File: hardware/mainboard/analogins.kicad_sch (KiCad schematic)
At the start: 27 parts, among them J102 CASTOR PITCH, J103 CASTOR DUTY, J111 POLLUX PITCH, J112 POLLUX DUTY, U13 MCP6004

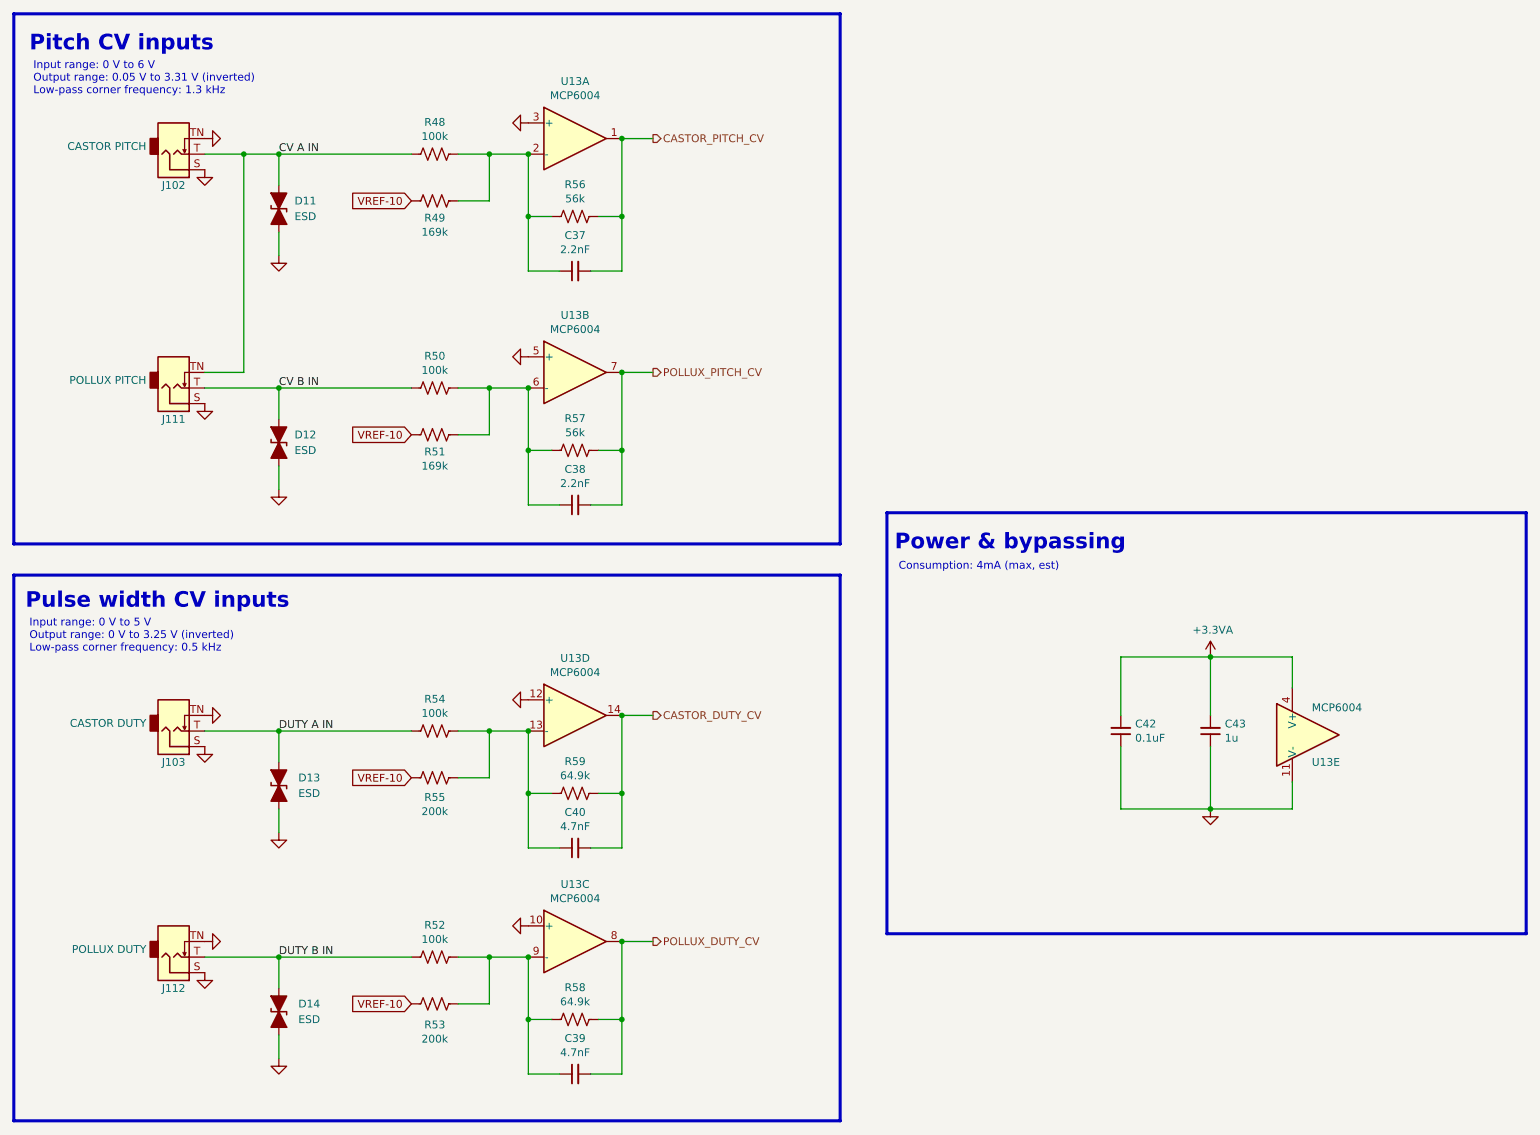
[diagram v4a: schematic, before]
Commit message: Reannotate schematic
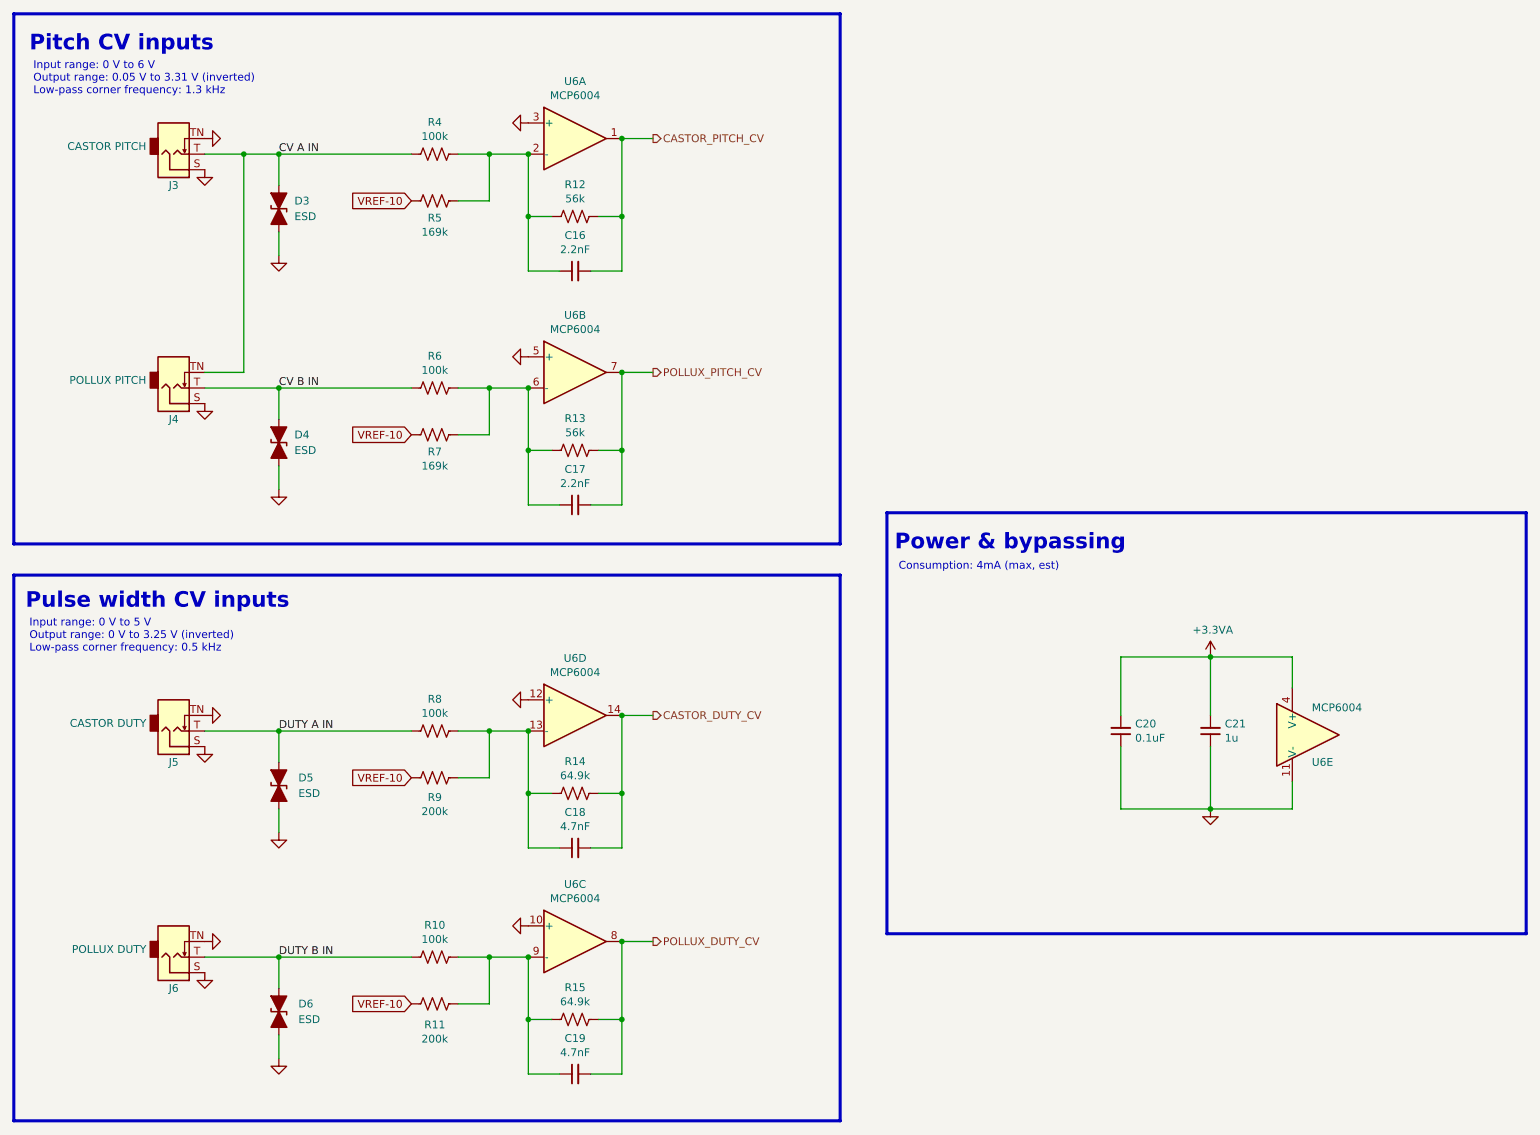
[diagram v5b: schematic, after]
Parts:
- renumbered C37 to C16, C38 to C17, C40 to C18, C39 to C19, C42 to C20, C43 to C21, D11 to D3, D12 to D4, D13 to D5, D14 to D6, J102 to J3, J111 to J4, J103 to J5, J112 to J6, R52 to R10, R53 to R11, R56 to R12, R57 to R13, R59 to R14, R58 to R15, R48 to R4, R49 to R5, R50 to R6, R51 to R7, R54 to R8, R55 to R9, U13 to U6

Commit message: Normalize component values
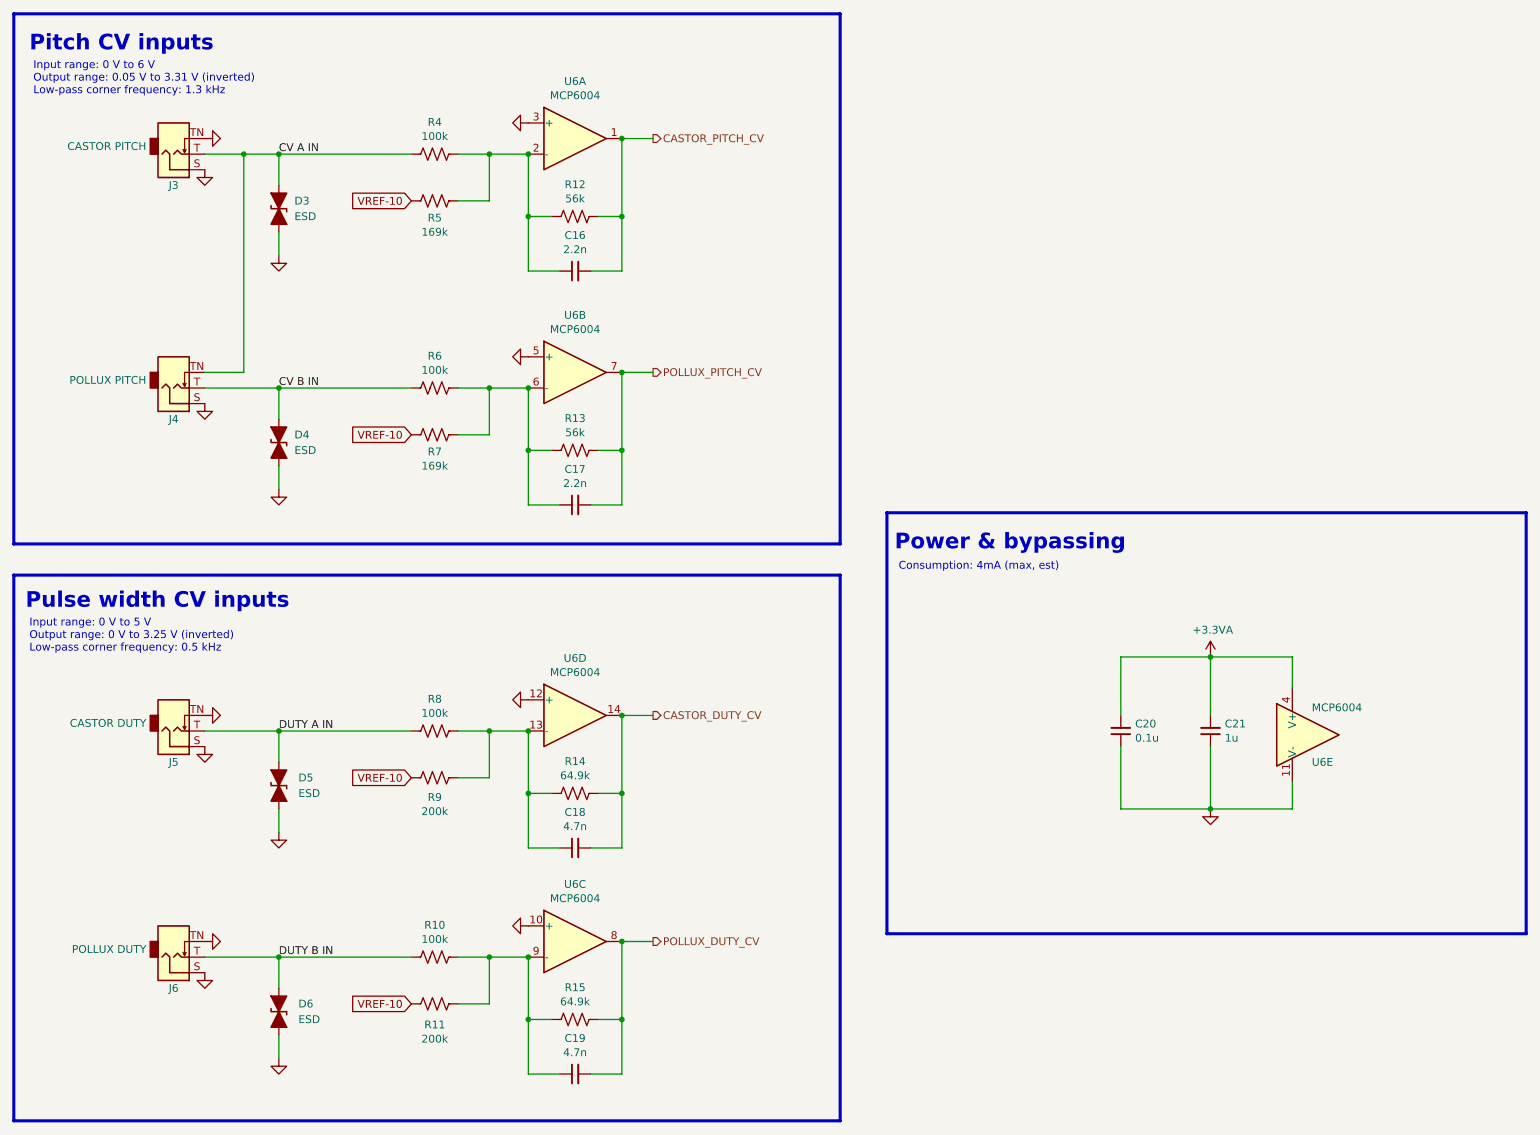
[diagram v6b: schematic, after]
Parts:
- C16, C17: value 2.2nF -> 2.2n
- C18, C19: value 4.7nF -> 4.7n
- C20: value 0.1uF -> 0.1u
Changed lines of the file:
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@@
     (in_bom yes) (on_board yes)
     (property "Reference" "C16" (id 0) (at 109.22 53.8734 90))
-    (property "Value" "2.2nF" (id 1) (at 109.22 56.1848 90))
+    (property "Value" "2.2n" (id 1) (at 109.22 56.1848 90))
     (property "Footprint" "Capacitor_SMD:C_0402_1005Metric_Pad0.74x0.62mm_HandSolder" (id 2) (at 109.22 59.69 0)
       (effects (font (size 1.27 1.27)) hide)
@@
     (in_bom yes) (on_board yes)
     (property "Reference" "C17" (id 0) (at 109.22 91.9734 90))
-    (property "Value" "2.2nF" (id 1) (at 109.22 94.2848 90))
+    (property "Value" "2.2n" (id 1) (at 109.22 94.2848 90))
     (property "Footprint" "Capacitor_SMD:C_0402_1005Metric_Pad0.74x0.62mm_HandSolder" (id 2) (at 109.22 97.79 0)
       (effects (font (size 1.27 1.27)) hide)
@@
     (in_bom yes) (on_board yes)
     (property "Reference" "C18" (id 0) (at 109.22 147.8534 90))
-    (property "Value" "4.7nF" (id 1) (at 109.22 150.1648 90))
+    (property "Value" "4.7n" (id 1) (at 109.22 150.1648 90))
     (property "Footprint" "Capacitor_SMD:C_0402_1005Metric_Pad0.74x0.62mm_HandSolder" (id 2) (at 109.22 153.67 0)
       (effects (font (size 1.27 1.27)) hide)
@@
     (in_bom yes) (on_board yes)
     (property "Reference" "C19" (id 0) (at 109.22 184.6834 90))
-    (property "Value" "4.7nF" (id 1) (at 109.22 186.9948 90))
+    (property "Value" "4.7n" (id 1) (at 109.22 186.9948 90))
     (property "Footprint" "Capacitor_SMD:C_0402_1005Metric_Pad0.74x0.62mm_HandSolder" (id 2) (at 109.22 190.5 0)
       (effects (font (size 1.27 1.27)) hide)
@@
       (effects (font (size 1.27 1.27)) (justify right))
     )
-    (property "Value" "0.1uF" (id 1) (at 200.4568 135.763 0)
+    (property "Value" "0.1u" (id 1) (at 200.4568 135.763 0)
       (effects (font (size 1.27 1.27)) (justify right))
     )

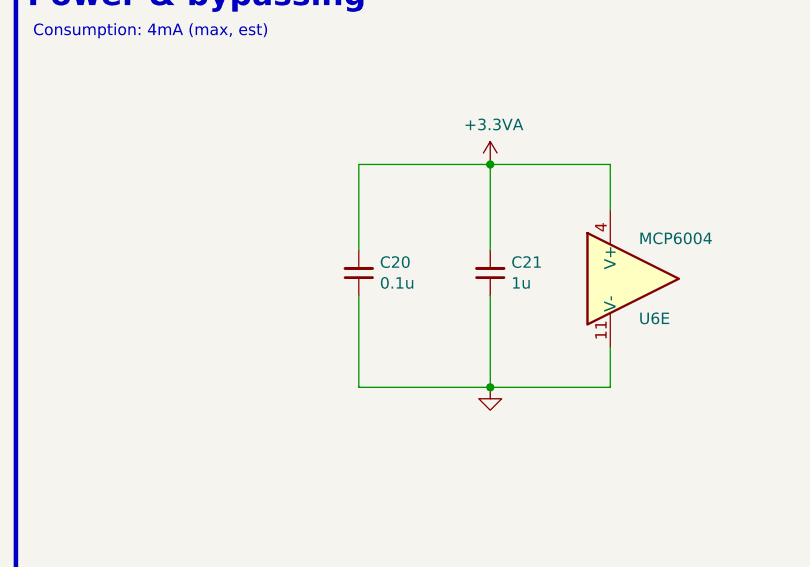
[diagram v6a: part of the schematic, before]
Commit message: Switch audio filter caps to 0603. Start auditing BOM
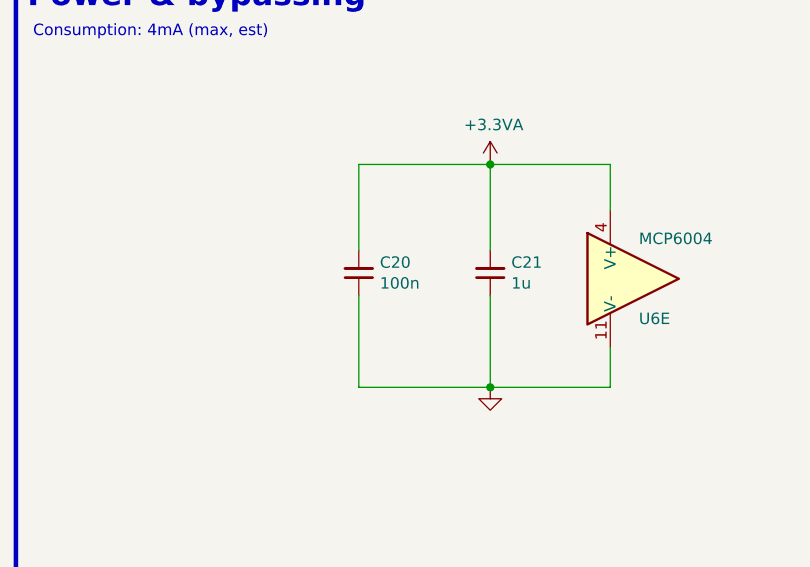
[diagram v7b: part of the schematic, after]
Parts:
- C16, C17: Reqs cv filter, 16v+ -> CV filter, 16 V; finalized yes -> (none); mpn CL10B222KC8WPNC -> (none); mpn alt GRM1885C1H222JA01J -> (none); mpn specs 10% 100v -> (none)
- C18, C19: Reqs cv filter, 16v+ -> CV filter, 16 V; finalized yes -> (none); mpn MF-CAP-0603-4.7nF -> (none); mpn alt GCD188R71H472MA01D -> (none); mpn specs 10% 50v -> (none)
- C20: value 0.1u -> 100n; Reqs bypass, 16v+ -> Bypass, 16 V; finalized yes -> (none); mpn MF-CAP-0603-0.1uF -> (none); mpn alt GCM188R91E104KA37D -> (none); mpn specs 10%, 25v -> (none)
- C21: Reqs bypass, 16v+ -> Bypass, 16 V; mpn MF-CAP-0603-1u -> (none); mpn alt GCM188R91E104KA37D -> (none); mpn specs 10%, 25v -> (none)
- D3, D4, D5, D6: Reqs (none) -> ESD diode, ceradiode, MOV, or small capacitor
- J3, J4, J5, J6: finalized (none) -> yes
- R10, R4, R6, R8: Reqs 0.5%, 2mW, analog front end -> Analog input, 0.5%, 2 mW; finalized yes -> (none); mpn RR0816P-104-D -> (none); mpn alt ERA-3AED104V -> (none); mpn specs 62mW, 0.5% -> (none)
- R11, R9: Reqs 1%, 1mW, analog front end -> Analog input, 0.5%, 1 mW; finalized yes -> (none); mpn RR0816P-204-D -> (none); mpn alt ERA-3AEB204V -> (none); mpn specs 62mW, 0.5% -> (none)
- R12, R13: Reqs 1%, 3mW, analog front end -> Analog input, 0.5%, 3 mW; finalized yes -> (none); mpn ERA-3AEB563V -> (none); mpn specs 100mW, 0.1% -> (none)
- R14, R15: Reqs 1%, 3mW, analog front end -> Analog input, 1%, 3 mW; finalized yes -> (none); mpn ERA-3AEB6492V -> (none); mpn specs 100mW, 0.1% -> (none)
- R5, R7: Reqs 1%, 1mW, analog front end -> Analog input, 0.5%, 1 mW; finalized yes -> (none); mpn RT0603DRD07169KL -> (none); mpn alt ERA-3AEB1693V -> (none); mpn specs 100mW, 0.5% -> (none)
